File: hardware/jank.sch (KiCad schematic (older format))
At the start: 65 parts, among them J1 usb-c_2.0, J2 AVR-ISP, SW0 SW_Push, U1 ATmega32U4-AU, U2 MP3202, Y1 16MHz

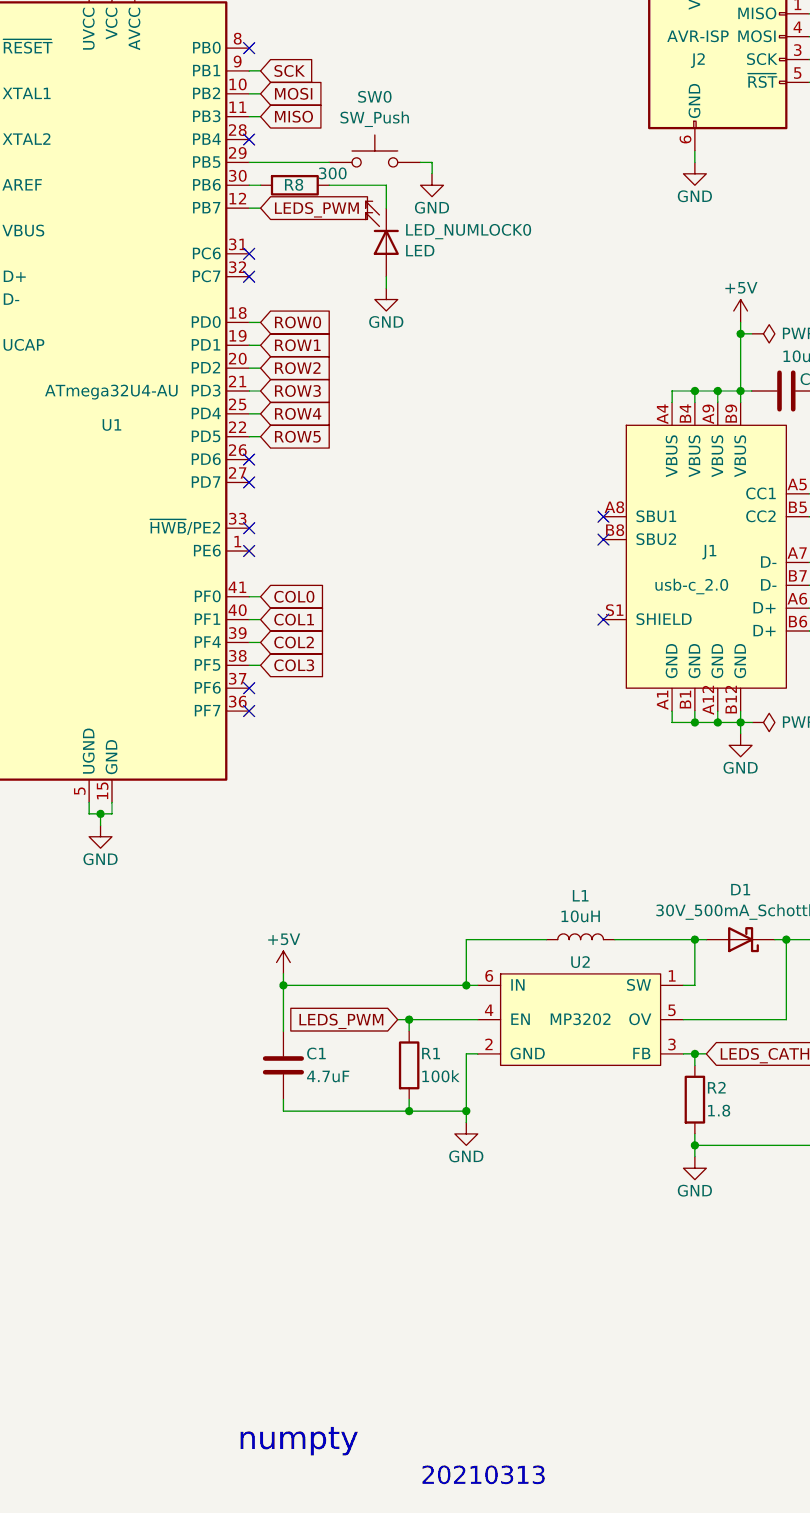
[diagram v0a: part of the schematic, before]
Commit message: Renaming project and repo from numpty to jank.
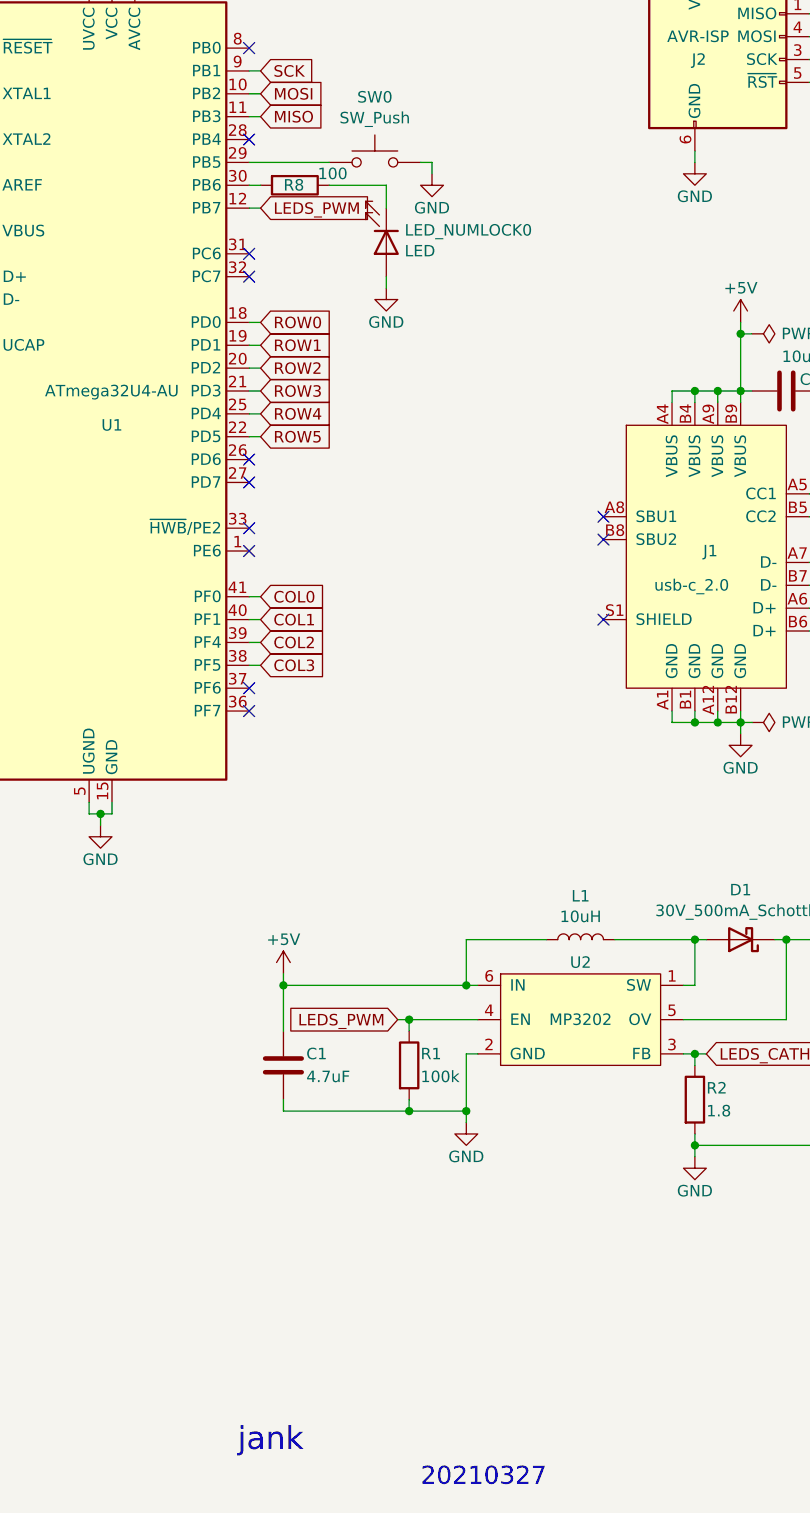
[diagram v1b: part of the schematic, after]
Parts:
- removed J1: usb-c_2.0, Connector_USB:USB_C_Receptacle_GCT_USB4085, symbol numpty:usb-c_2.0
- removed U2: MP3202, Package_TO_SOT_SMD:TSOT-23-6_HandSoldering, symbol numpty:MP3202
- added J1: usb-c_2.0, Connector_USB:USB_C_Receptacle_GCT_USB4085, symbol jank:usb-c_2.0
- added U2: MP3202, Package_TO_SOT_SMD:SOT-23-6_Handsoldering, symbol jank:MP3202
- L1: footprint numpty:SRN3010TA -> jank:SRN3010TA
- R8: value 300 -> 100
- SW_0, SW_1, SW_2, SW_3, SW_4, SW_5, SW_6, SW_7, SW_8, SW_9, SW_DIV0, SW_ENT0, SW_M0, SW_M1, SW_M2, SW_M3, SW_MIN0, SW_MUL0, SW_NL0, SW_PER0, SW_PLU0: footprint numpty:Gateron_LED_1.00u_Plate -> jank:Gateron_LED_1.00u_Plate
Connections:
- net +5V: now also J1.A4 (VBUS), J1.A9 (VBUS), J1.B4 (VBUS), J1.B9 (VBUS), U2.6 (IN)
- net GND: now also J1.A1 (GND), J1.A12 (GND), J1.B1 (GND), J1.B12 (GND), U2.2 (GND)
- net LEDS_ANODE: now also U2.5 (OV)
- net LEDS_CATHODE: now also U2.3 (FB)
- net LEDS_PWM: now also U2.4 (EN)
- net at R3.2: now also J1.A5 (CC1)
- net at R6.2: now also J1.A6 (D+), J1.B6 (D+)
- net at R5.2: now also J1.A7 (D-), J1.B7 (D-)
- net at R4.2: now also J1.B5 (CC2)
- net at D1.2 (A), L1.2: now also U2.1 (SW)
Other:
- note added: "20210327"
- note added: "jank"
- note removed: "20210313"
- note removed: "numpty"
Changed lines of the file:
@@
 F 0 "SW_M0" H 1800 2100 50  0000 C CNN
 F 1 "KEY_LED" H 1800 2000 50  0000 C CNN
-F 2 "numpty:Gateron_LED_1.00u_Plate" H 1800 2050 50  0001 C CNN
+F 2 "jank:Gateron_LED_1.00u_Plate" H 1800 2050 50  0001 C CNN
 F 3 "~" H 1800 2050 50  0001 C CNN
 	1    1800 1750
-	1    0    0    -1
-$EndComp
-$Comp
-L numpty:MP3202 U2
-U 1 1 6045DD88
-P 8850 5600
-F 0 "U2" H 8850 5850 50  0000 C CNN
-F 1 "MP3202" H 8850 5600 50  0000 C CNN
-F 2 "Package_TO_SOT_SMD:TSOT-23-6_HandSoldering" H 8850 5600 50  0001 C CNN
-F 3 "" H 8850 5600 50  0001 C CNN
-	1    8850 5600
 	1    0    0    -1
 $EndComp
@@
 $EndComp
 $Comp
-L numpty:usb-c_2.0 J1
-U 1 1 604568E4
-P 9400 3550
-F 0 "J1" H 9450 3550 50  0000 R CNN
-F 1 "usb-c_2.0" H 9500 3400 50  0000 R CNN
-F 2 "Connector_USB:USB_C_Receptacle_GCT_USB4085" H 9400 3550 50  0001 C CNN
-F 3 "" H 9400 3550 50  0001 C CNN
-	1    9400 3550
-	1    0    0    -1
-$EndComp
-$Comp
 L Device:D D_M0
 U 1 1 60459174
@@
 F 0 "SW_M1" H 2800 2100 50  0000 C CNN
 F 1 "KEY_LED" H 2800 2000 50  0000 C CNN
-F 2 "numpty:Gateron_LED_1.00u_Plate" H 2800 2050 50  0001 C CNN
+F 2 "jank:Gateron_LED_1.00u_Plate" H 2800 2050 50  0001 C CNN
 F 3 "~" H 2800 2050 50  0001 C CNN
 	1    2800 1750
@@
 F 0 "SW_NL0" H 1800 3100 50  0000 C CNN
 F 1 "KEY_LED" H 1800 3000 50  0000 C CNN
-F 2 "numpty:Gateron_LED_1.00u_Plate" H 1800 3050 50  0001 C CNN
+F 2 "jank:Gateron_LED_1.00u_Plate" H 1800 3050 50  0001 C CNN
 F 3 "~" H 1800 3050 50  0001 C CNN
 	1    1800 2750
@@
 F 0 "SW_M2" H 3800 2100 50  0000 C CNN
 F 1 "KEY_LED" H 3800 2000 50  0000 C CNN
-F 2 "numpty:Gateron_LED_1.00u_Plate" H 3800 2050 50  0001 C CNN
+F 2 "jank:Gateron_LED_1.00u_Plate" H 3800 2050 50  0001 C CNN
 F 3 "~" H 3800 2050 50  0001 C CNN
 	1    3800 1750
@@
 F 0 "SW_M3" H 4800 2100 50  0000 C CNN
 F 1 "KEY_LED" H 4800 2000 50  0000 C CNN
-F 2 "numpty:Gateron_LED_1.00u_Plate" H 4800 2050 50  0001 C CNN
+F 2 "jank:Gateron_LED_1.00u_Plate" H 4800 2050 50  0001 C CNN
 F 3 "~" H 4800 2050 50  0001 C CNN
 	1    4800 1750
@@
 F 0 "SW_DIV0" H 2800 3100 50  0000 C CNN
 F 1 "KEY_LED" H 2800 3000 50  0000 C CNN
-F 2 "numpty:Gateron_LED_1.00u_Plate" H 2800 3050 50  0001 C CNN
+F 2 "jank:Gateron_LED_1.00u_Plate" H 2800 3050 50  0001 C CNN
 F 3 "~" H 2800 3050 50  0001 C CNN
 	1    2800 2750
@@
 F 0 "SW_MUL0" H 3800 3100 50  0000 C CNN
 F 1 "KEY_LED" H 3800 3000 50  0000 C CNN
-F 2 "numpty:Gateron_LED_1.00u_Plate" H 3800 3050 50  0001 C CNN
+F 2 "jank:Gateron_LED_1.00u_Plate" H 3800 3050 50  0001 C CNN
 F 3 "~" H 3800 3050 50  0001 C CNN
 	1    3800 2750
@@
 F 0 "SW_MIN0" H 4800 3100 50  0000 C CNN
 F 1 "KEY_LED" H 4800 3000 50  0000 C CNN
-F 2 "numpty:Gateron_LED_1.00u_Plate" H 4800 3050 50  0001 C CNN
+F 2 "jank:Gateron_LED_1.00u_Plate" H 4800 3050 50  0001 C CNN
 F 3 "~" H 4800 3050 50  0001 C CNN
 	1    4800 2750
@@
 F 0 "SW_7" H 1800 4100 50  0000 C CNN
 F 1 "KEY_LED" H 1800 4000 50  0000 C CNN
-F 2 "numpty:Gateron_LED_1.00u_Plate" H 1800 4050 50  0001 C CNN
+F 2 "jank:Gateron_LED_1.00u_Plate" H 1800 4050 50  0001 C CNN
 F 3 "~" H 1800 4050 50  0001 C CNN
 	1    1800 3750
@@
 F 0 "SW_8" H 2800 4100 50  0000 C CNN
 F 1 "KEY_LED" H 2800 4000 50  0000 C CNN
-F 2 "numpty:Gateron_LED_1.00u_Plate" H 2800 4050 50  0001 C CNN
+F 2 "jank:Gateron_LED_1.00u_Plate" H 2800 4050 50  0001 C CNN
 F 3 "~" H 2800 4050 50  0001 C CNN
 	1    2800 3750
@@
 F 0 "SW_9" H 3800 4100 50  0000 C CNN
 F 1 "KEY_LED" H 3800 4000 50  0000 C CNN
-F 2 "numpty:Gateron_LED_1.00u_Plate" H 3800 4050 50  0001 C CNN
+F 2 "jank:Gateron_LED_1.00u_Plate" H 3800 4050 50  0001 C CNN
 F 3 "~" H 3800 4050 50  0001 C CNN
 	1    3800 3750
@@
 F 0 "SW_PLU0" H 4800 4100 50  0000 C CNN
 F 1 "KEY_LED" H 4800 4000 50  0000 C CNN
-F 2 "numpty:Gateron_LED_1.00u_Plate" H 4800 4050 50  0001 C CNN
+F 2 "jank:Gateron_LED_1.00u_Plate" H 4800 4050 50  0001 C CNN
 F 3 "~" H 4800 4050 50  0001 C CNN
 	1    4800 3750
@@
 F 0 "SW_4" H 1800 5100 50  0000 C CNN
 F 1 "KEY_LED" H 1800 5000 50  0000 C CNN
-F 2 "numpty:Gateron_LED_1.00u_Plate" H 1800 5050 50  0001 C CNN
+F 2 "jank:Gateron_LED_1.00u_Plate" H 1800 5050 50  0001 C CNN
 F 3 "~" H 1800 5050 50  0001 C CNN
 	1    1800 4750
@@
 F 0 "SW_5" H 2800 5100 50  0000 C CNN
 F 1 "KEY_LED" H 2800 5000 50  0000 C CNN
-F 2 "numpty:Gateron_LED_1.00u_Plate" H 2800 5050 50  0001 C CNN
+F 2 "jank:Gateron_LED_1.00u_Plate" H 2800 5050 50  0001 C CNN
 F 3 "~" H 2800 5050 50  0001 C CNN
 	1    2800 4750
@@
 F 0 "SW_6" H 3800 5100 50  0000 C CNN
 F 1 "KEY_LED" H 3800 5000 50  0000 C CNN
-F 2 "numpty:Gateron_LED_1.00u_Plate" H 3800 5050 50  0001 C CNN
+F 2 "jank:Gateron_LED_1.00u_Plate" H 3800 5050 50  0001 C CNN
 F 3 "~" H 3800 5050 50  0001 C CNN
 	1    3800 4750
@@
 F 0 "SW_1" H 1800 6100 50  0000 C CNN
 F 1 "KEY_LED" H 1800 6000 50  0000 C CNN
-F 2 "numpty:Gateron_LED_1.00u_Plate" H 1800 6050 50  0001 C CNN
+F 2 "jank:Gateron_LED_1.00u_Plate" H 1800 6050 50  0001 C CNN
 F 3 "~" H 1800 6050 50  0001 C CNN
 	1    1800 5750
@@
 F 0 "SW_2" H 2800 6100 50  0000 C CNN
 F 1 "KEY_LED" H 2800 6000 50  0000 C CNN
-F 2 "numpty:Gateron_LED_1.00u_Plate" H 2800 6050 50  0001 C CNN
+F 2 "jank:Gateron_LED_1.00u_Plate" H 2800 6050 50  0001 C CNN
 F 3 "~" H 2800 6050 50  0001 C CNN
 	1    2800 5750
@@
 F 0 "SW_3" H 3800 6100 50  0000 C CNN
 F 1 "KEY_LED" H 3800 6000 50  0000 C CNN
-F 2 "numpty:Gateron_LED_1.00u_Plate" H 3800 6050 50  0001 C CNN
+F 2 "jank:Gateron_LED_1.00u_Plate" H 3800 6050 50  0001 C CNN
 F 3 "~" H 3800 6050 50  0001 C CNN
 	1    3800 5750
@@
 F 0 "SW_ENT0" H 4800 6100 50  0000 C CNN
 F 1 "KEY_LED" H 4800 6000 50  0000 C CNN
-F 2 "numpty:Gateron_LED_1.00u_Plate" H 4800 6050 50  0001 C CNN
+F 2 "jank:Gateron_LED_1.00u_Plate" H 4800 6050 50  0001 C CNN
 F 3 "~" H 4800 6050 50  0001 C CNN
 	1    4800 5750
@@
 F 0 "SW_0" H 1800 7100 50  0000 C CNN
 F 1 "KEY_LED" H 1800 7000 50  0000 C CNN
-F 2 "numpty:Gateron_LED_1.00u_Plate" H 1800 7050 50  0001 C CNN
+F 2 "jank:Gateron_LED_1.00u_Plate" H 1800 7050 50  0001 C CNN
 F 3 "~" H 1800 7050 50  0001 C CNN
 	1    1800 6750
@@
 F 0 "SW_PER0" H 3800 7100 50  0000 C CNN
 F 1 "KEY_LED" H 3800 7000 50  0000 C CNN
-F 2 "numpty:Gateron_LED_1.00u_Plate" H 3800 7050 50  0001 C CNN
+F 2 "jank:Gateron_LED_1.00u_Plate" H 3800 7050 50  0001 C CNN
 F 3 "~" H 3800 7050 50  0001 C CNN
 	1    3800 6750
@@
 F 0 "L1" V 9040 5250 50  0000 C CNN
 F 1 "10uH" V 8950 5250 50  0000 C CNN
-F 2 "numpty:SRN3010TA" H 8850 5250 50  0001 C CNN
+F 2 "jank:SRN3010TA" H 8850 5250 50  0001 C CNN
 F 3 "~" H 8850 5250 50  0001 C CNN
 	1    8850 5250
@@
 P 7600 1950
 F 0 "R8" V 7600 1900 50  0000 L CNN
-F 1 "300" V 7550 2050 50  0000 L CNN
+F 1 "100" V 7550 2050 50  0000 L CNN
 F 2 "Resistor_SMD:R_1206_3216Metric_Pad1.42x1.75mm_HandSolder" V 7530 1950 50  0001 C CNN
 F 3 "~" H 7600 1950 50  0001 C CNN
@@
 NoConn ~ 7400 4250
 Text Notes 7350 7500 0    100  ~ 0
-numpty
+jank
 Text Notes 8150 7650 0    79   ~ 0
-20210313
+20210327
 Text Notes 10550 7650 0    79   ~ 0
 0
@@
 Wire Wire Line
 	8000 2350 8000 2400
+$Comp
+L jank:MP3202 U2
+U 1 1 60607415
+P 8850 5600
+F 0 "U2" H 8850 5850 50  0000 C CNN
+F 1 "MP3202" H 8850 5600 50  0000 C CNN
+F 2 "Package_TO_SOT_SMD:SOT-23-6_Handsoldering" H 8850 5600 50  0001 C CNN
+F 3 "" H 8850 5600 50  0001 C CNN
+	1    8850 5600
+	1    0    0    -1
+$EndComp
+$Comp
+L jank:usb-c_2.0 J1
+U 1 1 60608422
+P 9400 3550
+F 0 "J1" H 9450 3550 50  0000 R CNN
+F 1 "usb-c_2.0" H 9500 3400 50  0000 R CNN
+F 2 "Connector_USB:USB_C_Receptacle_GCT_USB4085" H 9400 3550 50  0001 C CNN
+F 3 "" H 9400 3550 50  0001 C CNN
+	1    9400 3550
+	1    0    0    -1
+$EndComp
 $EndSCHEMATC
